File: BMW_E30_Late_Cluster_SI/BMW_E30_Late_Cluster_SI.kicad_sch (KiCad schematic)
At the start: 0 parts

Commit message: Added Project Files + Updates
Added project files for SI LED daughter board and speedometer board. Started on reverse engineering schematic for late model SI board.

Also updated some formatting on the nexus board schematic.
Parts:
- added J5: Nexus Connector, symbol Connector:Conn_01x19_Pin
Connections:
- new net +12_T15: J5.5 (Pin_5)
- new net +12_T30: J5.8 (Pin_8)
- new net EG_1+: J5.15 (Pin_15)
- new net EG_1-: J5.14 (Pin_14)
- new net EG_2+: J5.12 (Pin_12)
- new net EG_2-: J5.13 (Pin_13)
- new net Eng_temp_sensor: J5.3 (Pin_3)
- new net Engine_spd_input: J5.9 (Pin_9)
- new net Fuel_rate_input: J5.10 (Pin_10)
- new net GNDPWR: J5.7 (Pin_7)
- new net SI_RST: J5.4 (Pin_4)
- new net Tach_1+: J5.16 (Pin_16)
- new net Tach_1-: J5.17 (Pin_17)
- new net Tach_2+: J5.18 (Pin_18)
- new net Tach_2-: J5.19 (Pin_19)
- new net Temp_+Ub: J5.1 (Pin_1)
- new net Temp_GND: J5.2 (Pin_2)
- new net Wheel_spd_output: J5.11 (Pin_11)
- no-connect marks 0 -> 1
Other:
- company: (none) -> Reagan Ansel

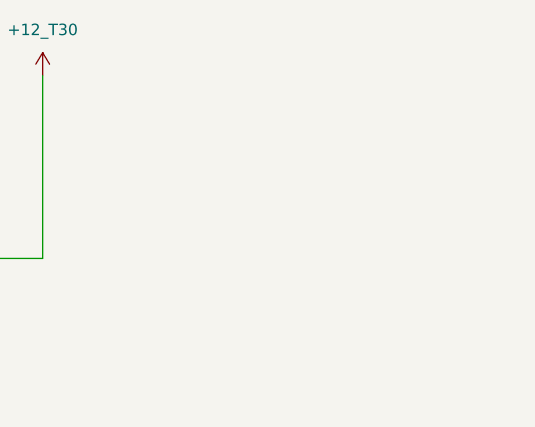
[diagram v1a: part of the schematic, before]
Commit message: Started SI Schematic
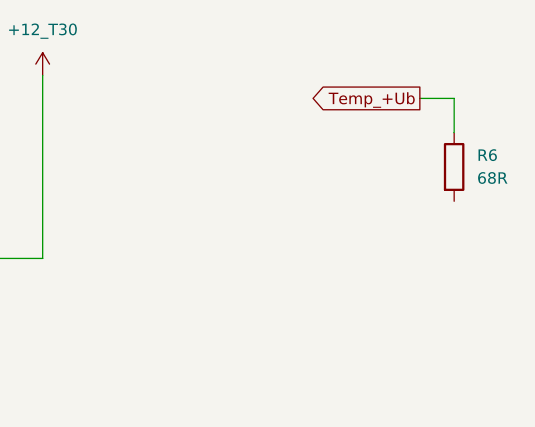
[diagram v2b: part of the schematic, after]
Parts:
- added R6: 68R, symbol Device:R
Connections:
- net Temp_+Ub: now also R6.1
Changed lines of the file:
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@@
+	(wire
+		(pts
+			(xy 119.38 30.48) (xy 119.38 26.67)
+		)
+		(stroke
+			(width 0)
+			(type default)
+		)
+	)
 	(wire
 		(pts
@@
 		(pts
 			(xy 73.66 44.45) (xy 34.29 44.45)
+		)
+		(stroke
+			(width 0)
+			(type default)
+		)
+	)
+	(wire
+		(pts
+			(xy 119.38 26.67) (xy 115.57 26.67)
 		)
 		(stroke
@@
 				)
 				(justify left)
+				(hide yes)
+			)
+		)
+	)
+	(global_label "Temp_+Ub"
+		(shape output)
+		(at 115.57 26.67 180)
+		(fields_autoplaced yes)
+		(effects
+			(font
+				(size 1.27 1.27)
+			)
+			(justify right)
+		)
+		(property "Intersheetrefs" "${INTERSHEET_REFS}"
+			(at 102.6668 26.67 0)
+			(effects
+				(font
+					(size 1.27 1.27)
+				)
+				(justify right)
 				(hide yes)
 			)
@@
 					(unit 1)
 				)
+			)
+		)
+	)
+	(symbol
+		(lib_id "Device:R")
+		(at 119.38 34.29 0)
+		(unit 1)
+		(exclude_from_sim no)
+		(in_bom yes)
+		(on_board yes)
+		(dnp no)
+		(fields_autoplaced yes)
+		(property "Reference" "R6"
+			(at 121.92 33.0199 0)
+			(effects
+				(font
+					(size 1.27 1.27)
+				)
+				(justify left)
+			)
+		)
+		(property "Value" "68R"
+			(at 121.92 35.5599 0)
+			(effects
+				(font
+					(size 1.27 1.27)
+				)
+				(justify left)
+			)
+		)
+		(property "Footprint" ""
+			(at 117.602 34.29 90)
+			(effects
+				(font
+					(size 1.27 1.27)
+				)
+				(hide yes)
+			)
+		)
+		(property "Datasheet" "~"
+			(at 119.38 34.29 0)
+			(effects
+				(font
+					(size 1.27 1.27)
+				)
+				(hide yes)
+			)
+		)
+		(property "Description" "5%, 0W5"
+			(at 119.38 34.29 0)
+			(effects
+				(font
+					(size 1.27 1.27)
+				)
+				(hide yes)
+			)
+		)
+		(pin "2"
+		)
+		(pin "1"
+		)
+		(instances
+			(project ""
+				(path "/00d578f4-1582-4e4e-9a07-e5462d38fb61"
+					(reference "R6")
+					(unit 1)
+				)

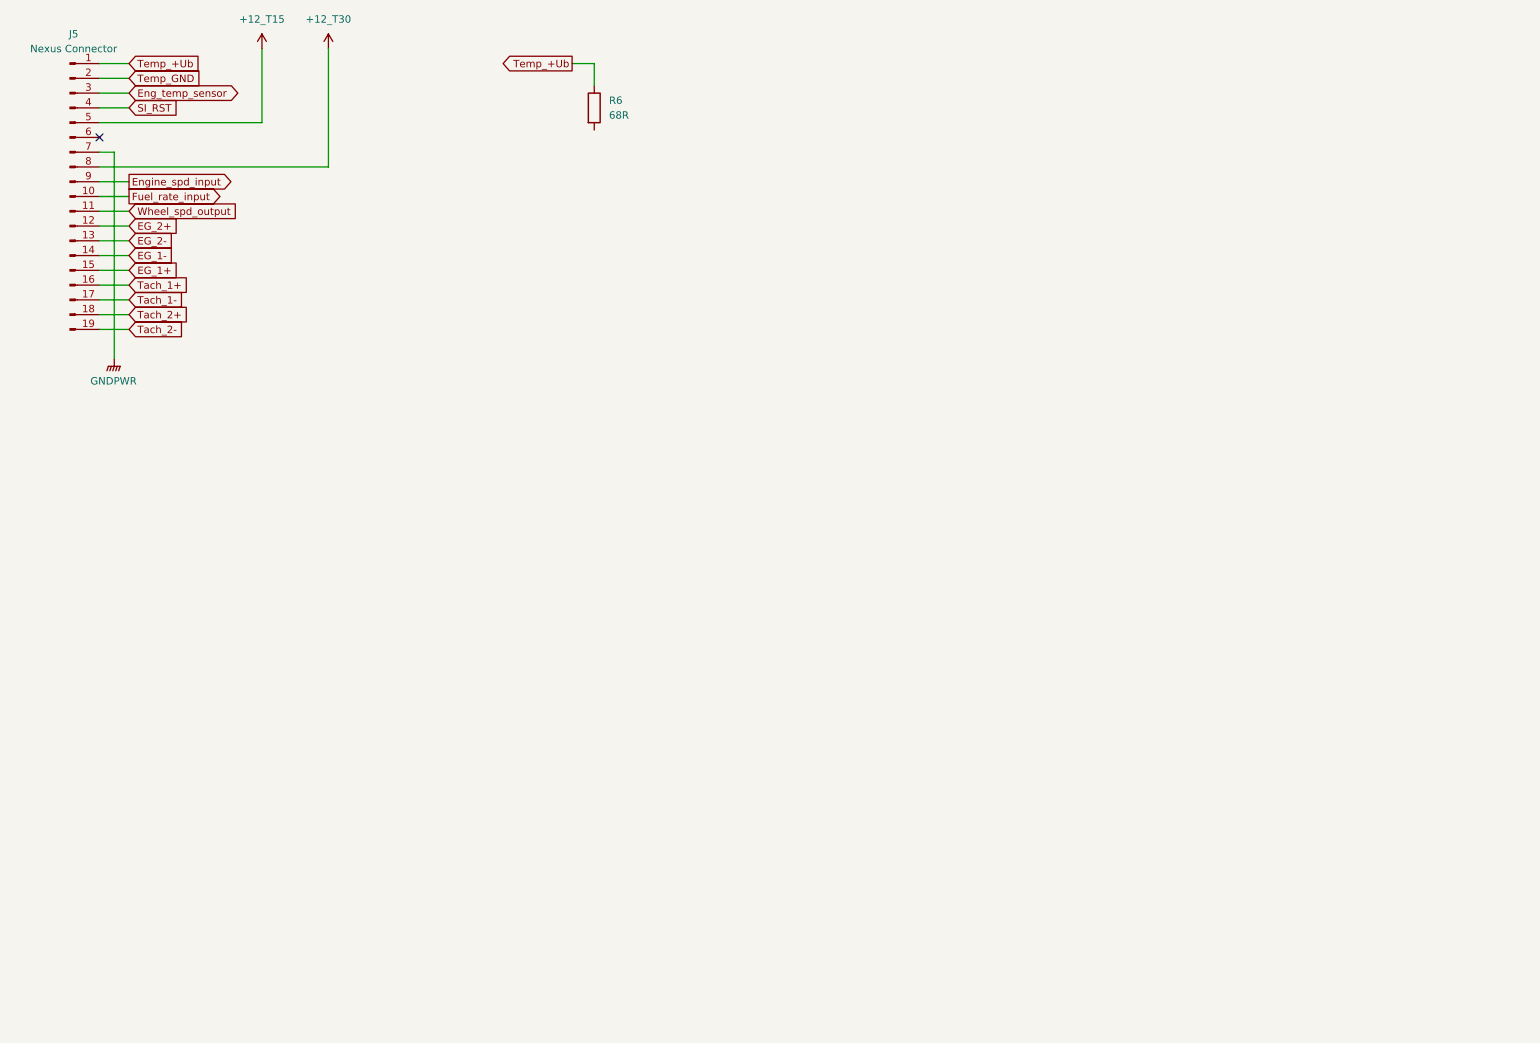
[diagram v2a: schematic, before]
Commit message: Board Updates
Added a few components + footprints.

Also added custom Connector V footprint, ported from Fabian Gmeiner's early model SI board project.
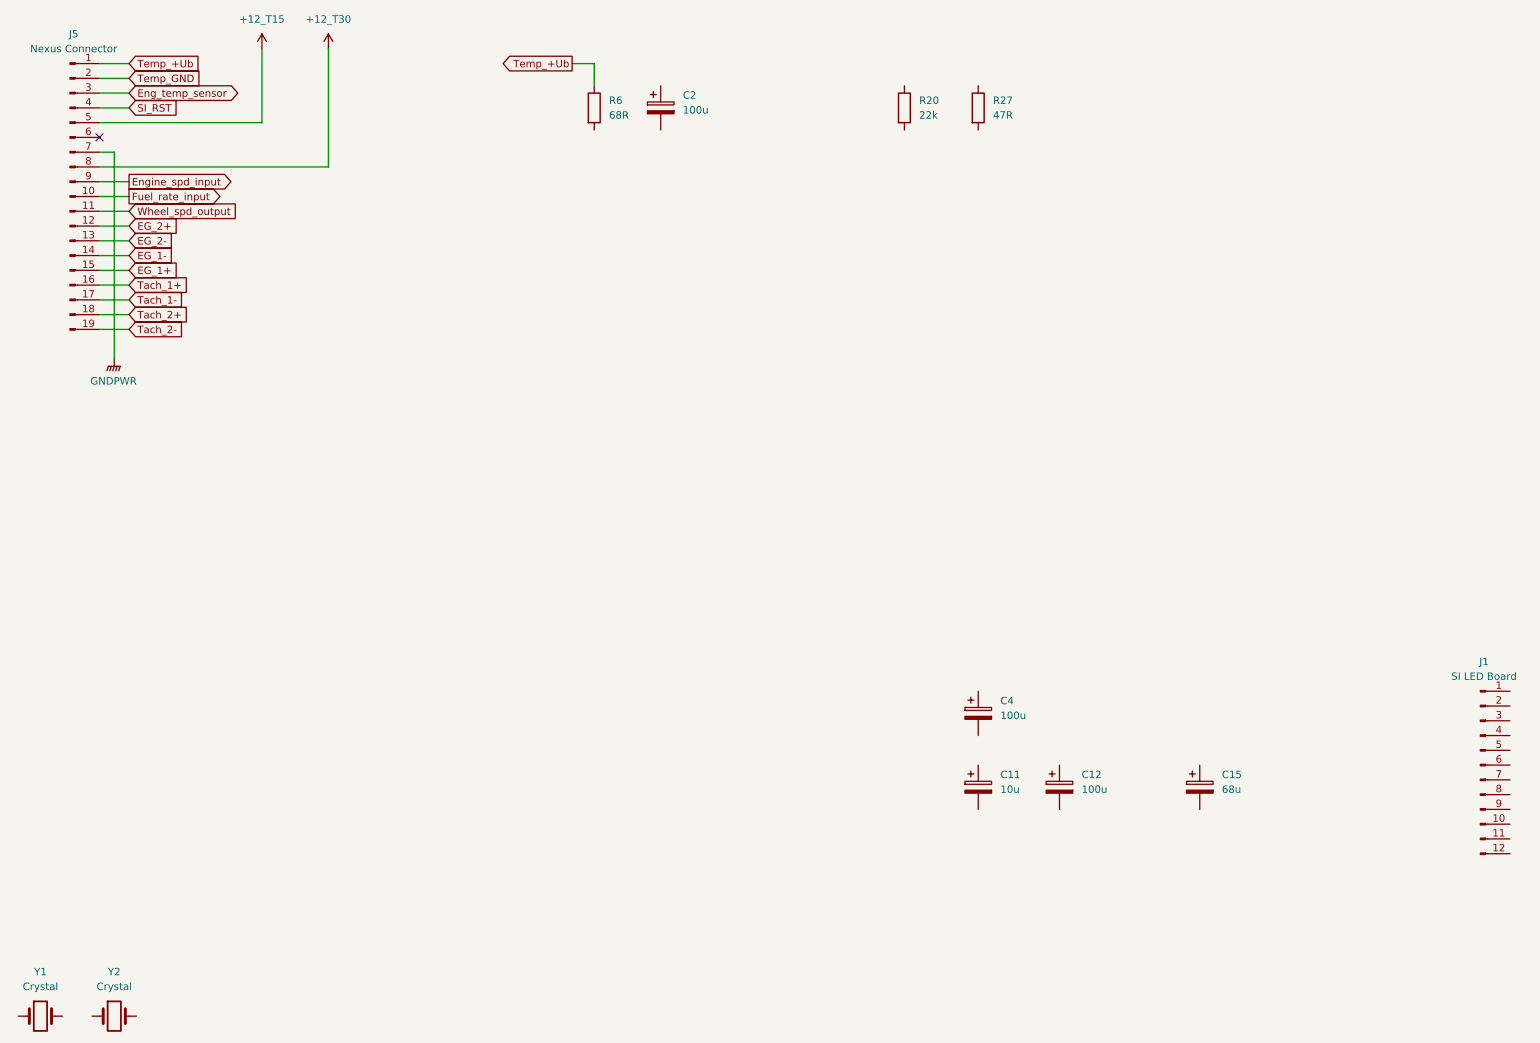
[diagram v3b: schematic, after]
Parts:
- added C11: 10u, Capacitor_THT:CP_Radial_Tantal_D9.0mm_P2.50mm, symbol Device:C_Polarized
- added C12, C2, C4: 100u, Capacitor_THT:CP_Axial_L18.0mm_D6.5mm_P25.00mm_Horizontal, symbol Device:C_Polarized
- added C15: 68u, Capacitor_THT:CP_Radial_Tantal_D5.5mm_P5.00mm, symbol Device:C_Polarized
- added J1: SI LED Board, Connector_PinHeader_2.54mm:PinHeader_1x12_P2.54mm_Vertical, symbol Connector:Conn_01x12_Pin
- added R20: 22k, Resistor_THT:R_Axial_DIN0207_L6.3mm_D2.5mm_P15.24mm_Horizontal, symbol Device:R
- added R27: 47R, Resistor_THT:R_Axial_DIN0516_L15.5mm_D5.0mm_P20.32mm_Horizontal, symbol Device:R
- added Y1: Crystal, Crystal:Crystal_HC18-U_Vertical, symbol Device:Crystal
- added Y2: Crystal, Crystal:Crystal_C38-LF_D3.0mm_L8.0mm_Horizontal, symbol Device:Crystal
- J5: footprint (none) -> BMW_Cluster_Connectors:E30_SI_Connector_Late_19Pin_P3.5
- R6: footprint (none) -> Resistor_THT:R_Axial_DIN0414_L11.9mm_D4.5mm_P20.32mm_Horizontal

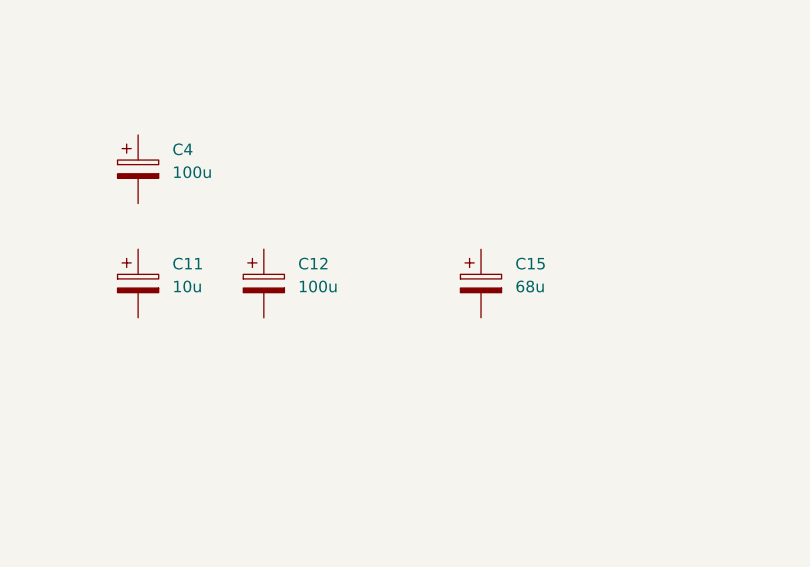
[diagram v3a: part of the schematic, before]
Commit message: Update to Schematic
Added Capacitor C13
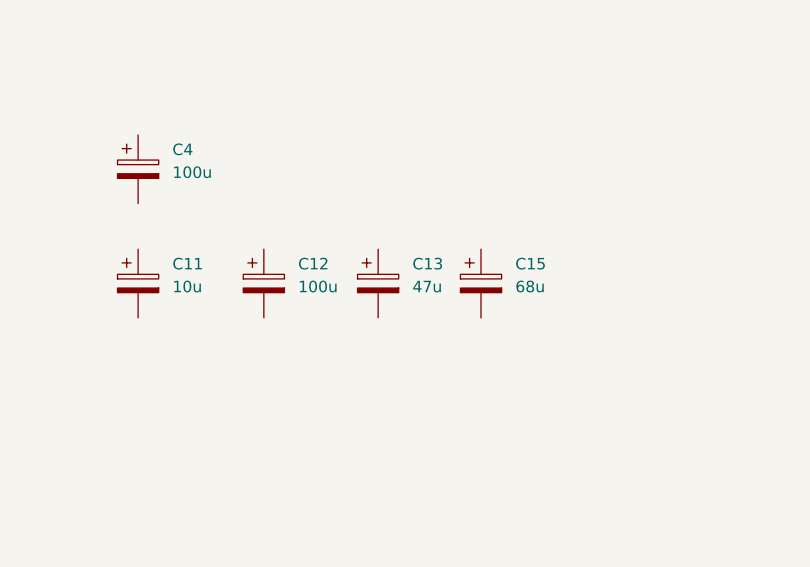
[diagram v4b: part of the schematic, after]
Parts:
- added C13: 47u, Capacitor_THT:CP_Radial_Tantal_D9.0mm_P2.50mm, symbol Device:C_Polarized
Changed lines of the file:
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@@
+	(symbol
+		(lib_id "Device:C_Polarized")
+		(at 212.09 151.13 0)
+		(unit 1)
+		(exclude_from_sim no)
+		(in_bom yes)
+		(on_board yes)
+		(dnp no)
+		(fields_autoplaced yes)
+		(property "Reference" "C13"
+			(at 215.9 148.9709 0)
+			(effects
+				(font
+					(size 1.27 1.27)
+				)
+				(justify left)
+			)
+		)
+		(property "Value" "47u"
+			(at 215.9 151.5109 0)
+			(effects
+				(font
+					(size 1.27 1.27)
+				)
+				(justify left)
+			)
+		)
+		(property "Footprint" "Capacitor_THT:CP_Radial_Tantal_D9.0mm_P2.50mm"
+			(at 213.0552 154.94 0)
+			(effects
+				(font
+					(size 1.27 1.27)
+				)
+				(hide yes)
+			)
+		)
+		(property "Datasheet" "~"
+			(at 212.09 151.13 0)
+			(effects
+				(font
+					(size 1.27 1.27)
+				)
+				(hide yes)
+			)
+		)
+		(property "Description" "16v"
+			(at 212.09 151.13 0)
+			(effects
+				(font
+					(size 1.27 1.27)
+				)
+				(hide yes)
+			)
+		)
+		(pin "2"
+		)
+		(pin "1"
+		)
+		(instances
+			(project "BMW_E30_Late_Cluster_SI"
+				(path "/00d578f4-1582-4e4e-9a07-e5462d38fb61"
+					(reference "C13")
+					(unit 1)
+				)
+			)
+		)
+	)
 	(symbol
 		(lib_id "Device:C_Polarized")

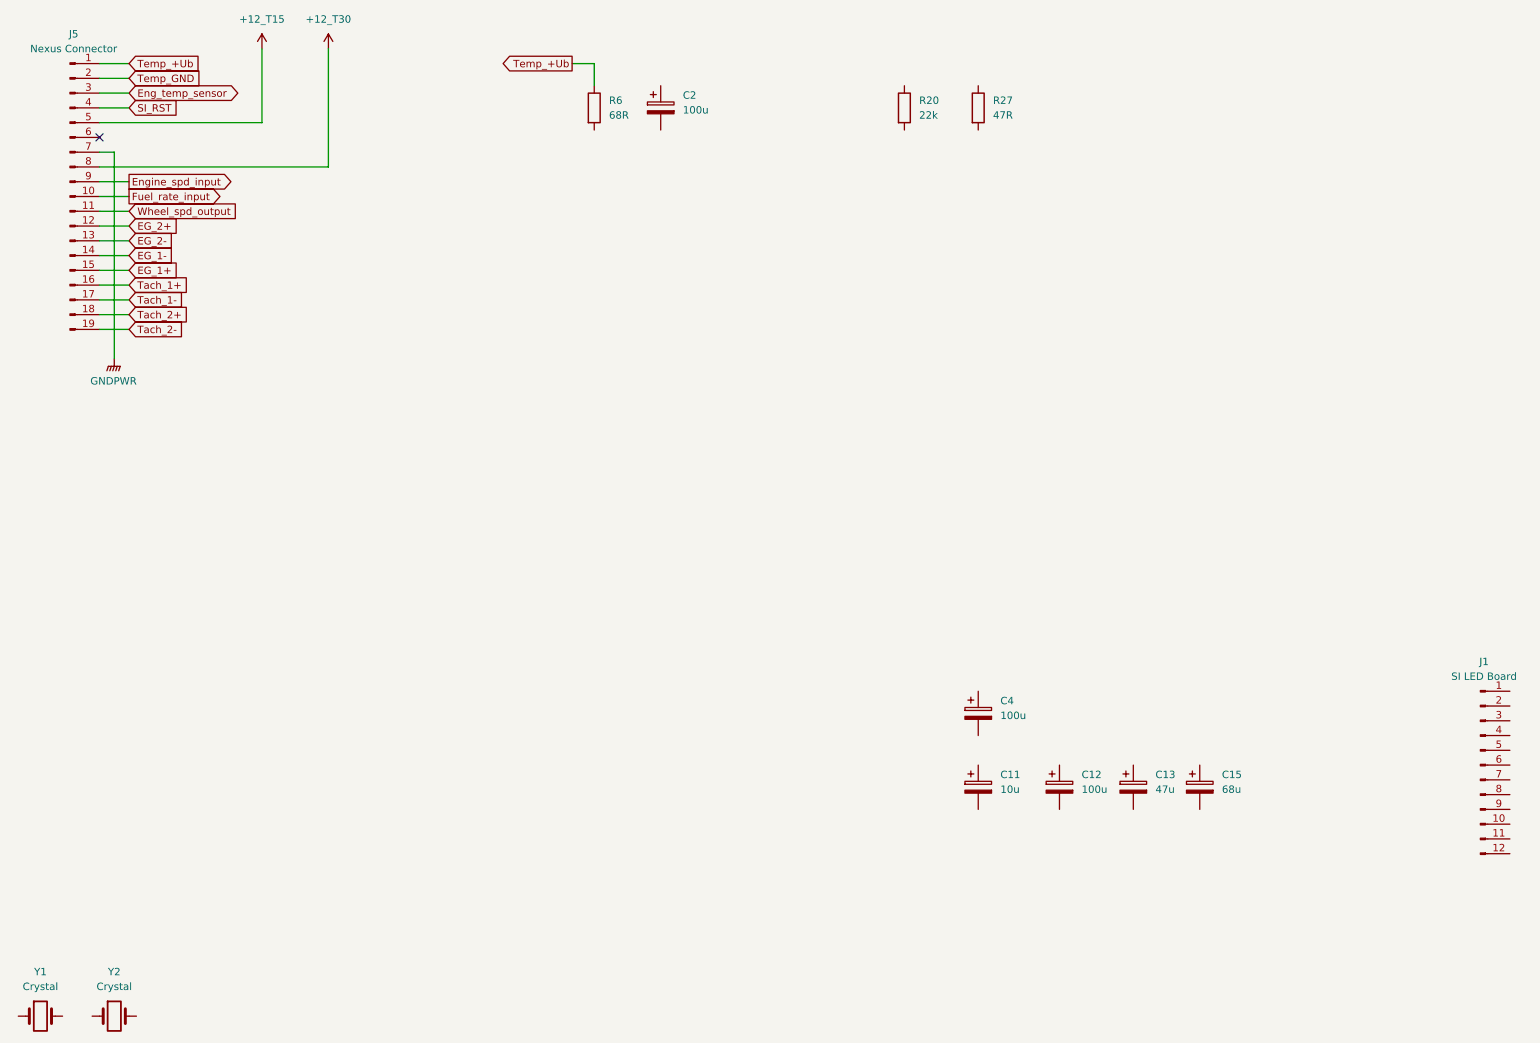
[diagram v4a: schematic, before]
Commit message: Schematic updates
Added all capacitors
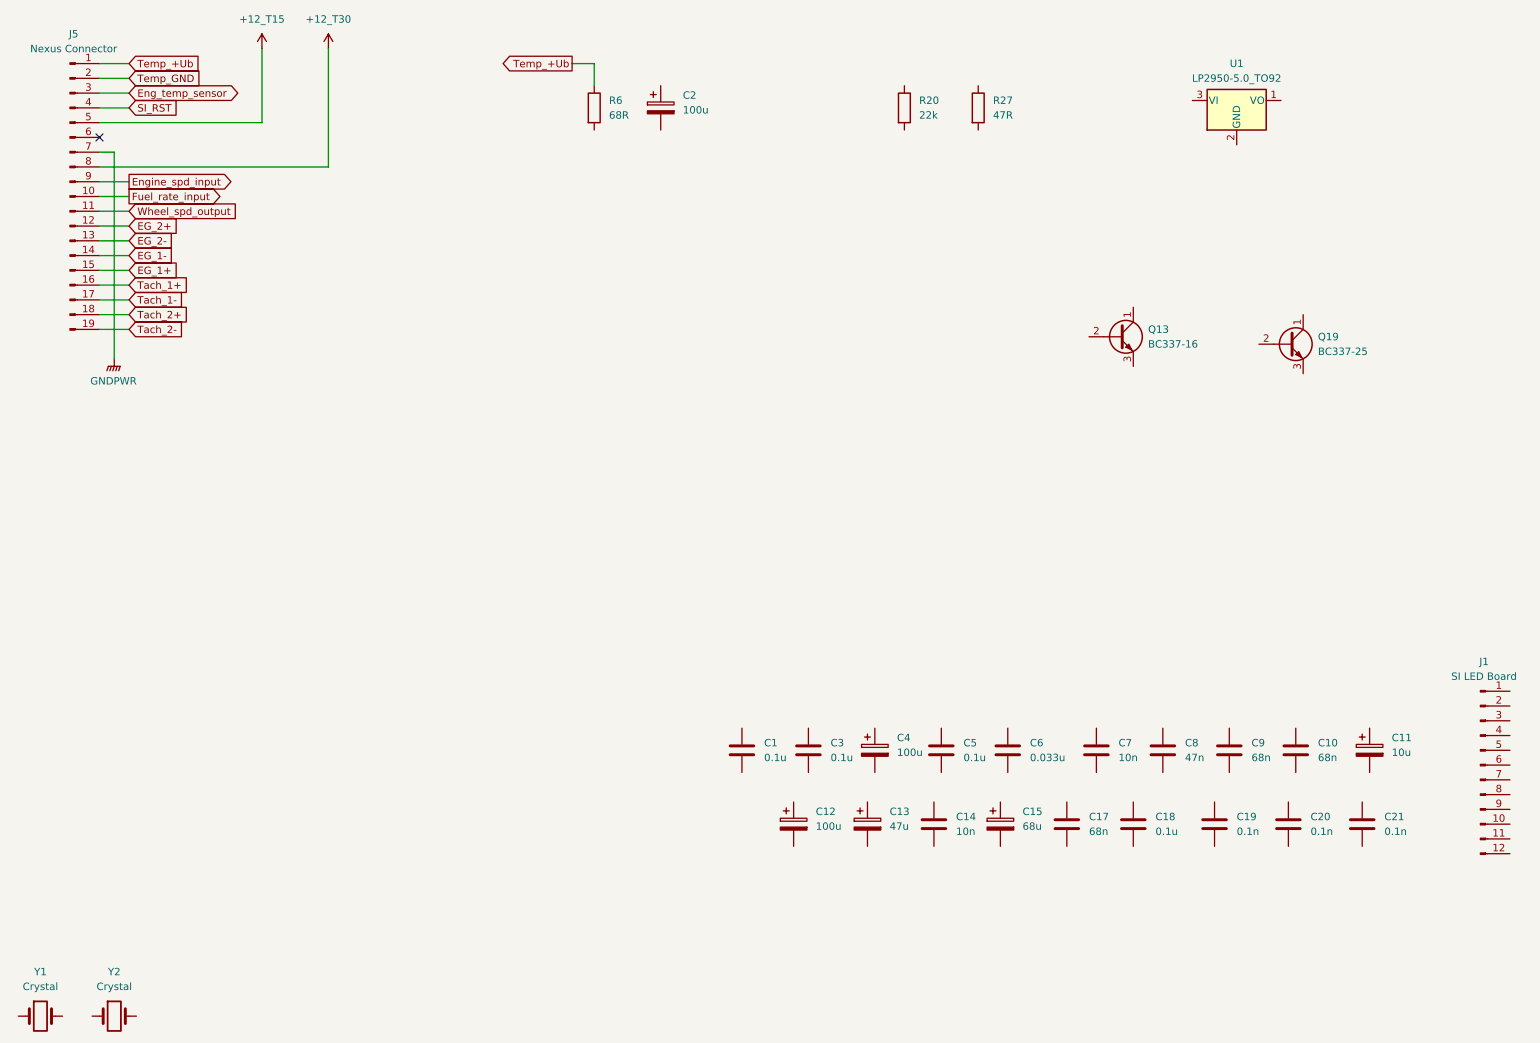
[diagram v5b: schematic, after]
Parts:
- added C1, C3: 0.1u, Capacitor_THT:C_Disc_D6.0mm_W2.5mm_P5.00mm, symbol Device:C
- added C10, C17, C9: 68n, Capacitor_THT:C_Disc_D6.0mm_W2.5mm_P5.00mm, symbol Device:C
- added C14: 10n, Capacitor_THT:C_Disc_D6.0mm_W2.5mm_P5.00mm, symbol Device:C
- added C18, C5: 0.1u, Capacitor_THT:C_Rect_L7.0mm_W2.0mm_P5.00mm, symbol Device:C
- added C19, C20, C21: 0.1n, Capacitor_THT:C_Disc_D6.0mm_W2.5mm_P5.00mm, symbol Device:C
- added C6: 0.033u, Capacitor_THT:C_Rect_L7.0mm_W2.0mm_P5.00mm, symbol Device:C
- added C7: 10n, Capacitor_THT:C_Rect_L7.0mm_W2.0mm_P5.00mm, symbol Device:C
- added C8: 47n, Capacitor_THT:C_Disc_D6.0mm_W2.5mm_P5.00mm, symbol Device:C
- added Q13: BC337-16, Package_TO_SOT_THT:TO-92_Inline, symbol Transistor_BJT:BC337
- added Q19: BC337-25, Package_TO_SOT_THT:TO-92_Inline, symbol Transistor_BJT:BC337
- added U1: LP2950-5.0_TO92, Package_TO_SOT_THT:TO-92_Inline, symbol Regulator_Linear:LP2950-5.0_TO92
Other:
- moved on the sheet: C11, C12, C13, C15, C4
